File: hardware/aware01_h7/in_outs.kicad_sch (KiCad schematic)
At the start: 33 parts, among them J11 InL, J13 OutR, J4 InL, J6 OutL, U10 NE5532DRG4, U9 NE5532DRG4

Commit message: update pcb
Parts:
- C43, C44, C49, C50: Manufacturer_Name (none) -> Vishay; Manufacturer_Part_Number (none) -> VJ0603Y104KFAAO; Mouser Part Number (none) -> 77-VJ0603Y104KFAAO
- C46: Manufacturer_Name (none) -> Walsin; Manufacturer_Part_Number (none) -> 0603N102J100CT; Mouser Part Number (none) -> 791-0603N102J100CT
- C53, C54: Manufacturer_Name (none) -> YAGEO; Manufacturer_Part_Number (none) -> CC0603JRNPO7BN221; Mouser Part Number (none) -> 603-CC0603JR7BN221
- J11, J13, J6: footprint Connector_Audio:Jack_3.5mm_QingPu_WQP-PJ398SM_Vertical_CircularHoles -> Eurorack:THONK_PJ398SM-12
- J4: value InL -> InR; footprint Connector_Audio:Jack_3.5mm_QingPu_WQP-PJ398SM_Vertical_CircularHoles -> Eurorack:THONK_PJ398SM-12
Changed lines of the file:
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@@
 		(shape input)
 		(at 163.83 133.35 180)
-		(fields_autoplaced yes)
 		(effects
 			(font
@@
 		(shape output)
 		(at 128.27 64.77 0)
-		(fields_autoplaced yes)
 		(effects
 			(font
@@
 		(shape output)
 		(at 128.27 133.35 0)
-		(fields_autoplaced yes)
 		(effects
 			(font
@@
 		(shape input)
 		(at 163.83 64.77 180)
-		(fields_autoplaced yes)
 		(effects
 			(font
@@
 			)
 		)
+		(property "Manufacturer_Name" " Vishay "
+			(at 29.21 87.63 0)
+			(effects
+				(font
+					(size 1.27 1.27)
+				)
+				(hide yes)
+			)
+		)
+		(property "Manufacturer_Part_Number" " VJ0603Y104KFAAO"
+			(at 29.21 87.63 0)
+			(effects
+				(font
+					(size 1.27 1.27)
+				)
+				(hide yes)
+			)
+		)
+		(property "Mouser Part Number" " 77-VJ0603Y104KFAAO "
+			(at 29.21 87.63 0)
+			(effects
+				(font
+					(size 1.27 1.27)
+				)
+				(hide yes)
+			)
+		)
 		(pin "2"
 		)
@@
 			)
 		)
+		(property "Manufacturer_Name" " Vishay "
+			(at 29.21 105.41 0)
+			(effects
+				(font
+					(size 1.27 1.27)
+				)
+				(hide yes)
+			)
+		)
+		(property "Manufacturer_Part_Number" " VJ0603Y104KFAAO"
+			(at 29.21 105.41 0)
+			(effects
+				(font
+					(size 1.27 1.27)
+				)
+				(hide yes)
+			)
+		)
+		(property "Mouser Part Number" " 77-VJ0603Y104KFAAO "
+			(at 29.21 105.41 0)
+			(effects
+				(font
+					(size 1.27 1.27)
+				)
+				(hide yes)
+			)
+		)
 		(pin "2"
 		)
@@
 			)
 		)
+		(property "Manufacturer_Name" "Walsin"
+			(at 91.44 105.41 0)
+			(effects
+				(font
+					(size 1.27 1.27)
+				)
+				(hide yes)
+			)
+		)
+		(property "Manufacturer_Part_Number" "0603N102J100CT "
+			(at 91.44 105.41 0)
+			(effects
+				(font
+					(size 1.27 1.27)
+				)
+				(hide yes)
+			)
+		)
+		(property "Mouser Part Number" " 791-0603N102J100CT "
+			(at 91.44 105.41 0)
+			(effects
+				(font
+					(size 1.27 1.27)
+				)
+				(hide yes)
+			)
+		)
 		(pin "2"
 		)
@@
 			)
 		)
-		(property "Footprint" "Connector_Audio:Jack_3.5mm_QingPu_WQP-PJ398SM_Vertical_CircularHoles"
+		(property "Footprint" "Eurorack:THONK_PJ398SM-12"
 			(at 247.65 67.31 0)
 			(effects
@@
 			)
 		)
+		(property "Manufacturer_Name" " Vishay "
+			(at 162.56 106.68 0)
+			(effects
+				(font
+					(size 1.27 1.27)
+				)
+				(hide yes)
+			)
+		)
+		(property "Manufacturer_Part_Number" " VJ0603Y104KFAAO"
+			(at 162.56 106.68 0)
+			(effects
+				(font
+					(size 1.27 1.27)
+				)
+				(hide yes)
+			)
+		)
+		(property "Mouser Part Number" " 77-VJ0603Y104KFAAO "
+			(at 162.56 106.68 0)
+			(effects
+				(font
+					(size 1.27 1.27)
+				)
+				(hide yes)
+			)
+		)
 		(pin "2"
 		)
@@
 			)
 		)
-		(property "Footprint" "Connector_Audio:Jack_3.5mm_QingPu_WQP-PJ398SM_Vertical_CircularHoles"
+		(property "Footprint" "Eurorack:THONK_PJ398SM-12"
 			(at 41.91 62.23 0)
 			(effects
@@
 			)
 		)
+		(property "Manufacturer_Name" " Vishay "
+			(at 162.56 88.9 0)
+			(effects
+				(font
+					(size 1.27 1.27)
+				)
+				(hide yes)
+			)
+		)
+		(property "Manufacturer_Part_Number" " VJ0603Y104KFAAO"
+			(at 162.56 88.9 0)
+			(effects
+				(font
+					(size 1.27 1.27)
+				)
+				(hide yes)
+			)
+		)
+		(property "Mouser Part Number" " 77-VJ0603Y104KFAAO "
+			(at 162.56 88.9 0)
+			(effects
+				(font
+					(size 1.27 1.27)
+				)
+				(hide yes)
+			)
+		)
 		(pin "2"
 		)
@@
 			)
 		)
+		(property "Manufacturer_Name" " YAGEO "
+			(at 209.55 107.95 0)
+			(effects
+				(font
+					(size 1.27 1.27)
+				)
+				(hide yes)
+			)
+		)
+		(property "Manufacturer_Part_Number" "CC0603JRNPO7BN221 "
+			(at 209.55 107.95 0)
+			(effects
+				(font
+					(size 1.27 1.27)
+				)
+				(hide yes)
+			)
+		)
+		(property "Mouser Part Number" "603-CC0603JR7BN221"
+			(at 209.55 107.95 0)
+			(effects
+				(font
+					(size 1.27 1.27)
+				)
+				(hide yes)
+			)
+		)
 		(pin "2"
 		)
@@
 			)
 		)
-		(property "Footprint" "Connector_Audio:Jack_3.5mm_QingPu_WQP-PJ398SM_Vertical_CircularHoles"
+		(property "Footprint" "Eurorack:THONK_PJ398SM-12"
 			(at 247.65 135.89 0)
 			(effects
@@
 			)
 		)
-		(property "Value" "InL"
+		(property "Value" "InR"
 			(at 41.275 137.16 0)
 			(effects
@@
 			)
 		)
-		(property "Footprint" "Connector_Audio:Jack_3.5mm_QingPu_WQP-PJ398SM_Vertical_CircularHoles"
+		(property "Footprint" "Eurorack:THONK_PJ398SM-12"
 			(at 41.91 130.81 0)
 			(effects
@@
 			(at 209.55 39.37 0)
 			(effects
+				(font
+					(size 1.27 1.27)
+				)
+				(hide yes)
+			)
+		)
+		(property "Manufacturer_Name" " YAGEO "
+			(at 209.55 39.37 0)
+			(effects
+				(font
+					(size 1.27 1.27)
+				)
+				(hide yes)
+			)
+		)
+		(property "Manufacturer_Part_Number" "CC0603JRNPO7BN221 "
+			(at 209.55 39.37 0)
+			(effects
+				(font
+					(size 1.27 1.27)
+				)
+				(hide yes)
+			)
+		)
+		(property "Mouser Part Number" "603-CC0603JR7BN221"
+			(at 209.55 39.37 0)
+			(effects

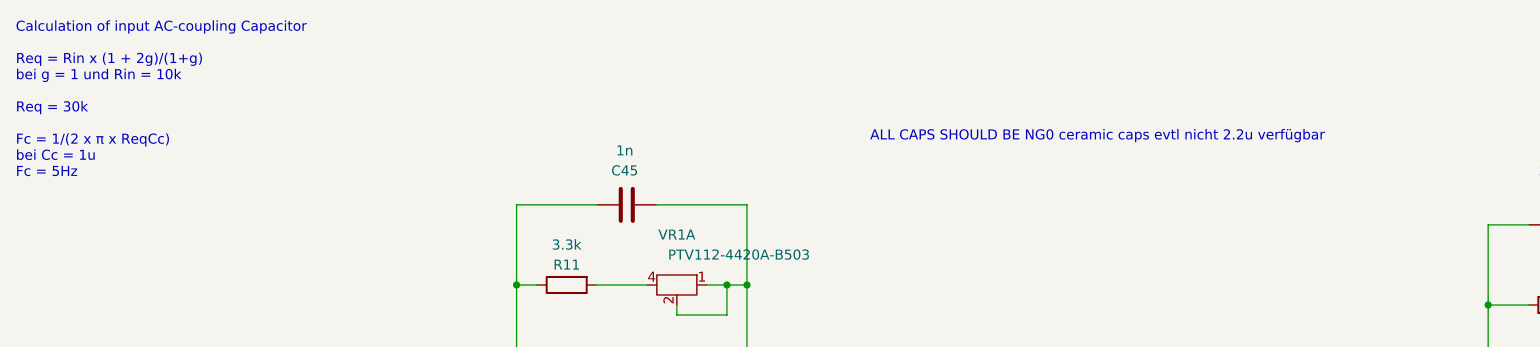
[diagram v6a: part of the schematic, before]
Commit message: change PWR to GND plane and reroute 3V3
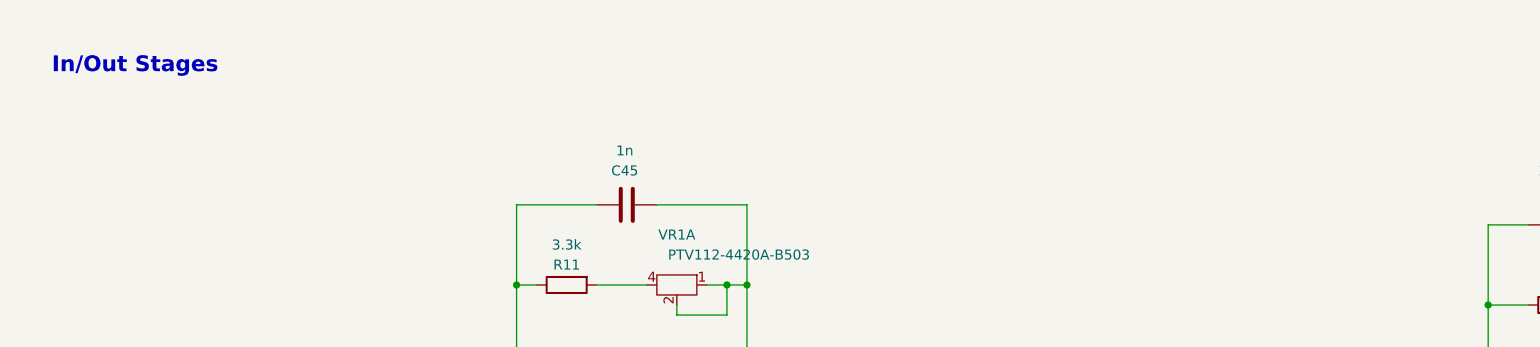
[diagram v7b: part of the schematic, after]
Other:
- note added: "In/Out Stages"
- note removed: "ALL CAPS SHOULD BE NG0 ceramic caps evtl nicht 2.2u verfügbar"
- note removed: "Calculation of input AC-coupling Capacitor Req = Rin x (1 + 2g)/(1+g) bei g = 1 und Rin = 10k Req = 30k Fc = 1/(2 x π x ReqCc) bei Cc = 1u Fc = 5Hz"
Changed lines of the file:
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@@
 		)
 	)
-	(text "ALL CAPS SHOULD BE NG0 ceramic caps evtl nicht 2.2u verfügbar"
+	(text "In/Out Stages"
 		(exclude_from_sim no)
-		(at 151.13 28.194 0)
+		(at 18.542 18.034 0)
 		(effects
 			(font
-				(size 1.27 1.27)
+				(size 2 2)
+				(thickness 0.4)
+				(bold yes)
 			)
+			(justify left top)
 		)
 	)
-	(text "Calculation of input AC-coupling Capacitor\n\nReq = Rin x (1 + 2g)/(1+g)\nbei g = 1 und Rin = 10k\n\nReq = 30k\n\nFc = 1/(2 x π x ReqCc)\nbei Cc = 1u\nFc = 5Hz\n"
-		(exclude_from_sim no)
-		(at 13.97 23.622 0)
-		(effects
-			(font
-				(size 1.27 1.27)
-			)
-			(justify left)
-		)
-	)

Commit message: update to rev 1.2
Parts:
- C43, C44, C49, C50: Manufacturer_Name Vishay -> Vishay
- C45: Manufacturer_Name (none) -> Walsin; Manufacturer_Part_Number (none) -> 0603N102J100CT; Mouser Part Number (none) -> 791-0603N102J100CT
- U10, U9: Manufacturer_Name https://www.ti.com/lit/ds/symlink/ne5532.pdf?ts=17370223077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 -> Texas Instruments
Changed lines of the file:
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@@
 			)
 		)
+		(property "Manufacturer_Name" "Walsin"
+			(at 91.44 36.83 0)
+			(effects
+				(font
+					(size 1.27 1.27)
+				)
+				(hide yes)
+			)
+		)
+		(property "Manufacturer_Part_Number" "0603N102J100CT "
+			(at 91.44 36.83 0)
+			(effects
+				(font
+					(size 1.27 1.27)
+				)
+				(hide yes)
+			)
+		)
+		(property "Mouser Part Number" " 791-0603N102J100CT "
+			(at 91.44 36.83 0)
+			(effects
+				(font
+					(size 1.27 1.27)
+				)
+				(hide yes)
+			)
+		)
 		(pin "2"
 		)
@@
 			)
 		)
-		(property "Manufacturer_Name" " Vishay "
+		(property "Manufacturer_Name" "Vishay "
 			(at 29.21 87.63 0)
 			(effects
@@
 			)
 		)
-		(property "Manufacturer_Name" " Vishay "
+		(property "Manufacturer_Name" "Vishay "
 			(at 29.21 105.41 0)
 			(effects
@@
 			)
 		)
-		(property "Manufacturer_Name" " Vishay "
+		(property "Manufacturer_Name" "Vishay "
 			(at 162.56 106.68 0)
 			(effects
@@
 			)
 		)
-		(property "Manufacturer_Name" "https://www.ti.com/lit/ds/symlink/ne5532.pdf?ts=1737022307701&ref_url=https%253A%252F%252Fwww.ti.com%252Fproduct%252FNE5532%253Futm_source%253Dgoogle%2526utm_medium%253Dcpc%2526utm_campaign%253Dasc-amps-null-44700045336317476_prodfolderdynamic-cpc-pf-google-eu_en_int%2526utm_content%253Dprodfolddynamic%2526ds_k%253DDYNAMIC+SEARCH+ADS%2526DCM%253Dyes%2526gad_source%253D1%2526gclid%253DCj0KCQiA-aK8BhCDARIsAL_-H9mYiaShwxHngsV995eTZ5z5kL5TUtr1-NxsW1eLHTpo7-NCtI5Cr20aApPfEALw_wcB%2526gclsrc%253Daw.ds"
+		(property "Manufacturer_Name" "Texas Instruments"
 			(at 88.9 133.35 0)
 			(effects
@@
 			)
 		)
-		(property "Manufacturer_Name" "https://www.ti.com/lit/ds/symlink/ne5532.pdf?ts=1737022307701&ref_url=https%253A%252F%252Fwww.ti.com%252Fproduct%252FNE5532%253Futm_source%253Dgoogle%2526utm_medium%253Dcpc%2526utm_campaign%253Dasc-amps-null-44700045336317476_prodfolderdynamic-cpc-pf-google-eu_en_int%2526utm_content%253Dprodfolddynamic%2526ds_k%253DDYNAMIC+SEARCH+ADS%2526DCM%253Dyes%2526gad_source%253D1%2526gclid%253DCj0KCQiA-aK8BhCDARIsAL_-H9mYiaShwxHngsV995eTZ5z5kL5TUtr1-NxsW1eLHTpo7-NCtI5Cr20aApPfEALw_wcB%2526gclsrc%253Daw.ds"
+		(property "Manufacturer_Name" "Texas Instruments"
 			(at 88.9 64.77 0)
 			(effects
@@
 			)
 		)
-		(property "Manufacturer_Name" " Vishay "
+		(property "Manufacturer_Name" "Vishay "
 			(at 162.56 88.9 0)
 			(effects
@@
 			)
 		)
-		(property "Manufacturer_Name" "https://www.ti.com/lit/ds/symlink/ne5532.pdf?ts=1737022307701&ref_url=https%253A%252F%252Fwww.ti.com%252Fproduct%252FNE5532%253Futm_source%253Dgoogle%2526utm_medium%253Dcpc%2526utm_campaign%253Dasc-amps-null-44700045336317476_prodfolderdynamic-cpc-pf-google-eu_en_int%2526utm_content%253Dprodfolddynamic%2526ds_k%253DDYNAMIC+SEARCH+ADS%2526DCM%253Dyes%2526gad_source%253D1%2526gclid%253DCj0KCQiA-aK8BhCDARIsAL_-H9mYiaShwxHngsV995eTZ5z5kL5TUtr1-NxsW1eLHTpo7-NCtI5Cr20aApPfEALw_wcB%2526gclsrc%253Daw.ds"
+		(property "Manufacturer_Name" "Texas Instruments"
 			(at 171.45 97.79 0)
 			(effects
@@
 			)
 		)
-		(property "Manufacturer_Name" "https://www.ti.com/lit/ds/symlink/ne5532.pdf?ts=1737022307701&ref_url=https%253A%252F%252Fwww.ti.com%252Fproduct%252FNE5532%253Futm_source%253Dgoogle%2526utm_medium%253Dcpc%2526utm_campaign%253Dasc-amps-null-44700045336317476_prodfolderdynamic-cpc-pf-google-eu_en_int%2526utm_content%253Dprodfolddynamic%2526ds_k%253DDYNAMIC+SEARCH+ADS%2526DCM%253Dyes%2526gad_source%253D1%2526gclid%253DCj0KCQiA-aK8BhCDARIsAL_-H9mYiaShwxHngsV995eTZ5z5kL5TUtr1-NxsW1eLHTpo7-NCtI5Cr20aApPfEALw_wcB%2526gclsrc%253Daw.ds"
+		(property "Manufacturer_Name" "Texas Instruments"
 			(at 212.09 67.31 0)
 			(effects
@@
 			)
 		)
-		(property "Manufacturer_Name" "https://www.ti.com/lit/ds/symlink/ne5532.pdf?ts=1737022307701&ref_url=https%253A%252F%252Fwww.ti.com%252Fproduct%252FNE5532%253Futm_source%253Dgoogle%2526utm_medium%253Dcpc%2526utm_campaign%253Dasc-amps-null-44700045336317476_prodfolderdynamic-cpc-pf-google-eu_en_int%2526utm_content%253Dprodfolddynamic%2526ds_k%253DDYNAMIC+SEARCH+ADS%2526DCM%253Dyes%2526gad_source%253D1%2526gclid%253DCj0KCQiA-aK8BhCDARIsAL_-H9mYiaShwxHngsV995eTZ5z5kL5TUtr1-NxsW1eLHTpo7-NCtI5Cr20aApPfEALw_wcB%2526gclsrc%253Daw.ds"
+		(property "Manufacturer_Name" "Texas Instruments"
 			(at 38.1 96.52 0)
 			(effects
@@
 			)
 		)
-		(property "Manufacturer_Name" "https://www.ti.com/lit/ds/symlink/ne5532.pdf?ts=1737022307701&ref_url=https%253A%252F%252Fwww.ti.com%252Fproduct%252FNE5532%253Futm_source%253Dgoogle%2526utm_medium%253Dcpc%2526utm_campaign%253Dasc-amps-null-44700045336317476_prodfolderdynamic-cpc-pf-google-eu_en_int%2526utm_content%253Dprodfolddynamic%2526ds_k%253DDYNAMIC+SEARCH+ADS%2526DCM%253Dyes%2526gad_source%253D1%2526gclid%253DCj0KCQiA-aK8BhCDARIsAL_-H9mYiaShwxHngsV995eTZ5z5kL5TUtr1-NxsW1eLHTpo7-NCtI5Cr20aApPfEALw_wcB%2526gclsrc%253Daw.ds"
+		(property "Manufacturer_Name" "Texas Instruments"
 			(at 212.09 135.89 0)
 			(effects
